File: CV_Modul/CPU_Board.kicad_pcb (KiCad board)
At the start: 4 copper layers, 65 x 100 mm, 123 parts, among them J101 Screw_Terminal_01x03, J102 Conn_02x01, J103 Conn_02x01, J104 Conn_01x08_Male, J105 Conn_02x09_Odd_Even, J106 Micro_SD_Card_Det, J107 Conn_01x06_Male, J108 Conn_02x01, J109 Conn_02x01, J110 Screw_Terminal_01x04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

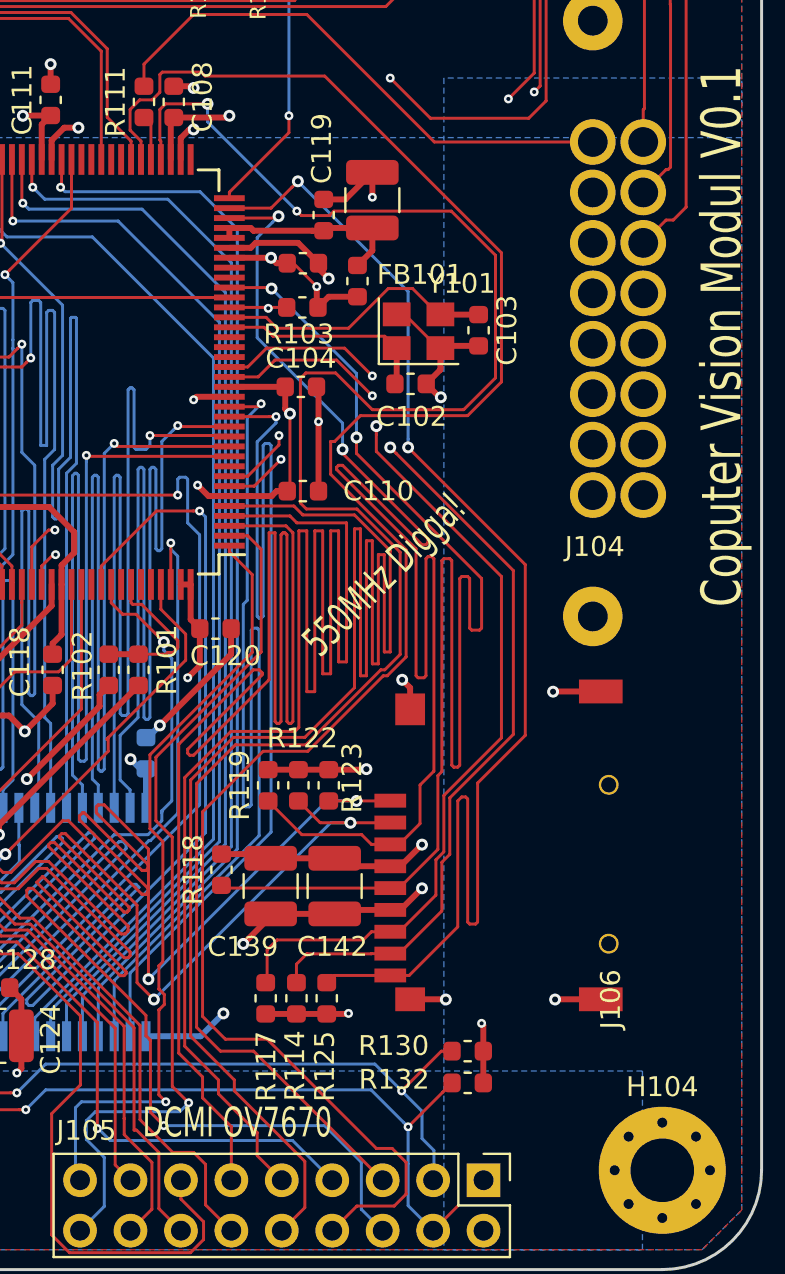
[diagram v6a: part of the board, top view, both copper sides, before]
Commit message: CV Modul Strong 1K Pulldown CAN Phy für Fast Mode. STEP Modelle hinzugefügt. Connector für Kamera etwas nach rechts verschoben
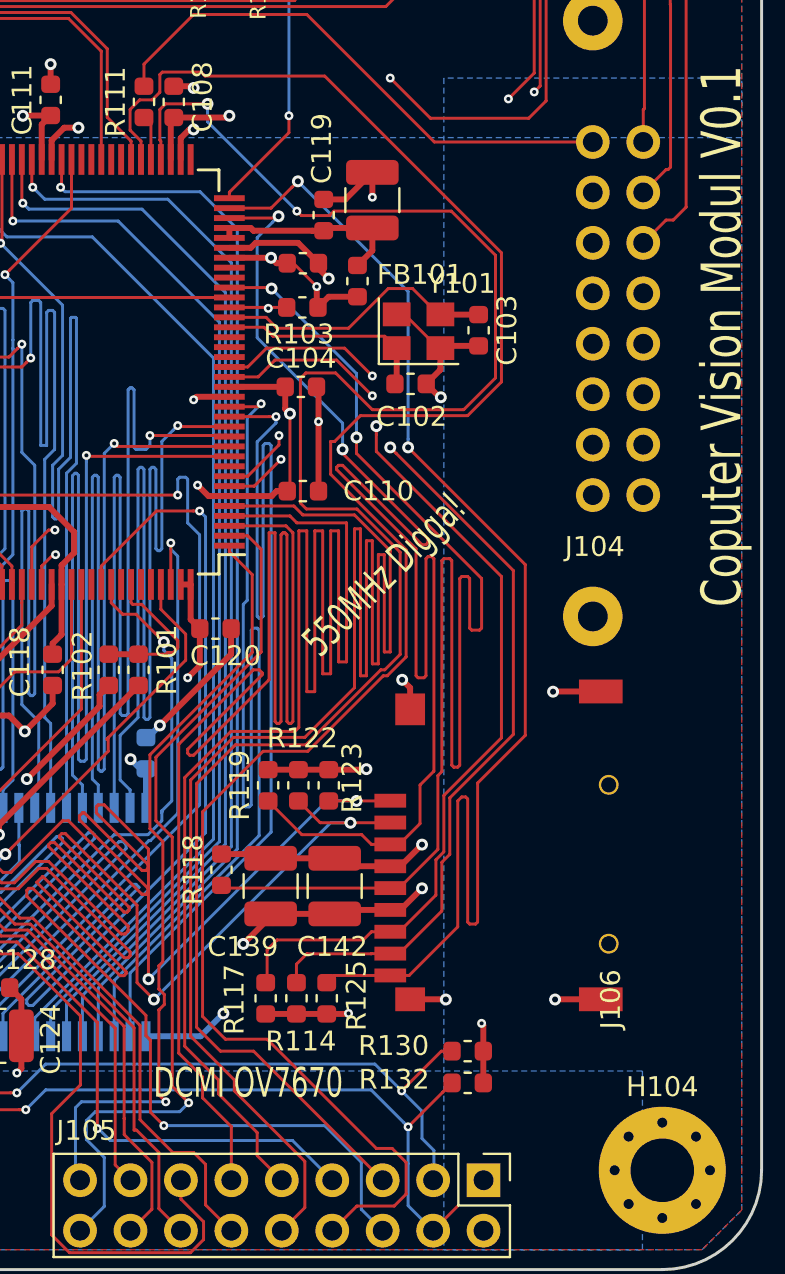
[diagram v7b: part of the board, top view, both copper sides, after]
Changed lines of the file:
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@@
     (add_net /NRST)
   )
+  (module ProjectFootprints:ST7789_Waveshare (layer F.Cu)
+    (at 126.5 111)
+    (fp_text reference J104 (at 0.1 2.6) (layer F.SilkS)
+      (effects (font (size 1 1) (thickness 0.15)))
+    )
+    (fp_text value Conn_01x08_Male (at -5 7.5) (layer F.Fab)
+      (effects (font (size 1 1) (thickness 0.15)))
+    )
+    (fp_line (start 2.5 -26.39) (end -55.5 -26.39) (layer Dwgs.User) (width 0.1))
+    (fp_line (start -55.5 -26.39) (end -55.5 8.61) (layer Dwgs.User) (width 0.1))
+    (fp_line (start -55.5 8.61) (end 2.5 8.61) (layer Dwgs.User) (width 0.1))
+    (fp_line (start 2.5 8.61) (end 2.5 -26.39) (layer Dwgs.User) (width 0.1))
+    (pad 16 thru_hole circle (at 2.54 0) (size 1.7 1.7) (drill 1) (layers *.Cu *.Mask))
+    (pad 15 thru_hole circle (at 2.54 -2.54) (size 1.7 1.7) (drill 1) (layers *.Cu *.Mask))
+    (pad 14 thru_hole circle (at 2.54 -5.08) (size 1.7 1.7) (drill 1) (layers *.Cu *.Mask))
+    (pad 13 thru_hole circle (at 2.54 -7.62) (size 1.7 1.7) (drill 1) (layers *.Cu *.Mask))
+    (pad 12 thru_hole circle (at 2.54 -10.16) (size 1.7 1.7) (drill 1) (layers *.Cu *.Mask))
+    (pad 11 thru_hole circle (at 2.54 -12.7) (size 1.7 1.7) (drill 1) (layers *.Cu *.Mask)
+      (net 58 /PA2))
+    (pad 10 thru_hole circle (at 2.54 -15.24) (size 1.7 1.7) (drill 1) (layers *.Cu *.Mask)
+      (net 106 /PC6))
+    (pad 9 thru_hole circle (at 2.54 -17.78) (size 1.7 1.7) (drill 1) (layers *.Cu *.Mask)
+      (net 9 /PC7))
+    (pad "" np_thru_hole circle (at -53 6.11) (size 3 3) (drill 1.5) (layers *.Cu *.Mask))
+    (pad "" np_thru_hole circle (at 0 6.11) (size 3 3) (drill 1.5) (layers *.Cu *.Mask))
+    (pad "" np_thru_hole circle (at -53 -23.89) (size 3 3) (drill 1.5) (layers *.Cu *.Mask))
+    (pad "" np_thru_hole circle (at 0 -23.89) (size 3 3) (drill 1.5) (layers *.Cu *.Mask))
+    (pad 8 thru_hole circle (at 0 -17.78) (size 1.7 1.7) (drill 1) (layers *.Cu *.Mask)
+      (net 26 /DISP_BL))
+    (pad 7 thru_hole circle (at 0 -15.24) (size 1.7 1.7) (drill 1) (layers *.Cu *.Mask)
+      (net 25 /DISP_RST))
+    (pad 6 thru_hole circle (at 0 -12.7) (size 1.7 1.7) (drill 1) (layers *.Cu *.Mask)
+      (net 24 /DISP_DC))
+    (pad 5 thru_hole circle (at 0 -10.16) (size 1.7 1.7) (drill 1) (layers *.Cu *.Mask)
+      (net 23 /DISP_CD))
+    (pad 4 thru_hole circle (at 0 -7.62) (size 1.7 1.7) (drill 1) (layers *.Cu *.Mask)
+      (net 22 /DISP_CLK))
+    (pad 3 thru_hole circle (at 0 -5.08) (size 1.7 1.7) (drill 1) (layers *.Cu *.Mask)
+      (net 21 /DISP_DIN))
+    (pad 2 thru_hole circle (at 0 -2.54) (size 1.7 1.7) (drill 1) (layers *.Cu *.Mask)
+      (net 1 GND))
+    (pad 1 thru_hole circle (at 0 0) (size 1.7 1.7) (drill 1) (layers *.Cu *.Mask)
+      (net 5 +3V3))
+  )
   (module Connector_PinHeader_2.54mm:PinHeader_2x09_P2.54mm_Vertical (layer F.Cu)
     (at 121 145.5 270)
@@
     (pad 18 thru_hole oval (at 2.54 20.32 270) (size 1.7 1.7) (drill 1) (layers *.Cu *.Mask)
       (net 41 /CAM_RESET))
-    (model ${KISYS3DMOD}/Connector_PinHeader_2.54mm.3dshapes/PinHeader_2x09_P2.54mm_Vertical.wrl
+    (model "${KIPRJMOD}/KiCAD_Library/STEP/18-Pin Shrouded Header (IDC) Straight.stp"
       (at (xyz 0 0 0))
       (scale (xyz 1 1 1))
-      (rotate (xyz 0 0 0))
+      (rotate (xyz 0 0 -90))
     )
   )
@@
     (fp_line (start 0 0) (end 1 0) (layer Dwgs.User) (width 0.12))
   )
-  (module ProjectFootprints:ST7789_Waveshare (layer F.Cu)
-    (at 126.5 111)
-    (fp_text reference J104 (at 0.1 2.6) (layer F.SilkS)
-      (effects (font (size 1 1) (thickness 0.15)))
-    )
-    (fp_text value Conn_01x08_Male (at -5 7.5) (layer F.Fab)
-      (effects (font (size 1 1) (thickness 0.15)))
-    )
-    (fp_line (start 2.5 -26.39) (end -55.5 -26.39) (layer Dwgs.User) (width 0.1))
-    (fp_line (start -55.5 -26.39) (end -55.5 8.61) (layer Dwgs.User) (width 0.1))
-    (fp_line (start -55.5 8.61) (end 2.5 8.61) (layer Dwgs.User) (width 0.1))
-    (fp_line (start 2.5 8.61) (end 2.5 -26.39) (layer Dwgs.User) (width 0.1))
-    (pad 16 thru_hole circle (at 2.54 0) (size 2.3 2.3) (drill 1.5) (layers *.Cu *.Mask))
-    (pad 15 thru_hole circle (at 2.54 -2.54) (size 2.3 2.3) (drill 1.5) (layers *.Cu *.Mask))
-    (pad 14 thru_hole circle (at 2.54 -5.08) (size 2.3 2.3) (drill 1.5) (layers *.Cu *.Mask))
-    (pad 13 thru_hole circle (at 2.54 -7.62) (size 2.3 2.3) (drill 1.5) (layers *.Cu *.Mask))
-    (pad 12 thru_hole circle (at 2.54 -10.16) (size 2.3 2.3) (drill 1.5) (layers *.Cu *.Mask))
-    (pad 11 thru_hole circle (at 2.54 -12.7) (size 2.3 2.3) (drill 1.5) (layers *.Cu *.Mask)
-      (net 58 /PA2))
-    (pad 10 thru_hole circle (at 2.54 -15.24) (size 2.3 2.3) (drill 1.5) (layers *.Cu *.Mask)
-      (net 106 /PC6))
-    (pad 9 thru_hole circle (at 2.54 -17.78) (size 2.3 2.3) (drill 1.5) (layers *.Cu *.Mask)
-      (net 9 /PC7))
-    (pad "" np_thru_hole circle (at -53 6.11) (size 3 3) (drill 1.5) (layers *.Cu *.Mask))
-    (pad "" np_thru_hole circle (at 0 6.11) (size 3 3) (drill 1.5) (layers *.Cu *.Mask))
-    (pad "" np_thru_hole circle (at -53 -23.89) (size 3 3) (drill 1.5) (layers *.Cu *.Mask))
-    (pad "" np_thru_hole circle (at 0 -23.89) (size 3 3) (drill 1.5) (layers *.Cu *.Mask))
-    (pad 8 thru_hole circle (at 0 -17.78) (size 2.3 2.3) (drill 1.5) (layers *.Cu *.Mask)
-      (net 26 /DISP_BL))
-    (pad 7 thru_hole circle (at 0 -15.24) (size 2.3 2.3) (drill 1.5) (layers *.Cu *.Mask)
-      (net 25 /DISP_RST))
-    (pad 6 thru_hole circle (at 0 -12.7) (size 2.3 2.3) (drill 1.5) (layers *.Cu *.Mask)
-      (net 24 /DISP_DC))
-    (pad 5 thru_hole circle (at 0 -10.16) (size 2.3 2.3) (drill 1.5) (layers *.Cu *.Mask)
-      (net 23 /DISP_CD))
-    (pad 4 thru_hole circle (at 0 -7.62) (size 2.3 2.3) (drill 1.5) (layers *.Cu *.Mask)
-      (net 22 /DISP_CLK))
-    (pad 3 thru_hole circle (at 0 -5.08) (size 2.3 2.3) (drill 1.5) (layers *.Cu *.Mask)
-      (net 21 /DISP_DIN))
-    (pad 2 thru_hole circle (at 0 -2.54) (size 2.3 2.3) (drill 1.5) (layers *.Cu *.Mask)
-      (net 1 GND))
-    (pad 1 thru_hole circle (at 0 0) (size 2.3 2.3) (drill 1.5) (layers *.Cu *.Mask)
-      (net 5 +3V3))
-  )
   (module ProjectFootprints:L_CommonModeChoke_Coilcraft_1812CAN (layer F.Cu)
     (at 105.6 66.2)
@@
     (pad 3 thru_hole circle (at 10 0 180) (size 2.1 2.1) (drill 1.1) (layers *.Cu *.Mask)
       (net 1 GND))
-    (model ${KISYS3DMOD}/TerminalBlock_RND.3dshapes/TerminalBlock_RND_205-00046_1x03_P5.00mm_Horizontal.wrl
-      (at (xyz 0 0 0))
+    (model ${KIPRJMOD}/KiCAD_Library/STEP/DG306-5.0-03P-12-00AH.STEP
+      (offset (xyz 12.5 -4.5 0))
       (scale (xyz 1 1 1))
-      (rotate (xyz 0 0 0))
+      (rotate (xyz -90 0 180))
     )
   )
@@
     (pad 4 thru_hole circle (at 15 0) (size 2.1 2.1) (drill 1.1) (layers *.Cu *.Mask)
       (net 109 /CAN_L))
-    (model ${KISYS3DMOD}/TerminalBlock_RND.3dshapes/TerminalBlock_RND_205-00047_1x04_P5.00mm_Horizontal.wrl
-      (at (xyz 0 0 0))
+    (model ${KIPRJMOD}/KiCAD_Library/STEP/DG306-5.0-04P-12-00AH.STEP
+      (offset (xyz 17.5 -4.5 0))
       (scale (xyz 1 1 1))
-      (rotate (xyz 0 0 0))
+      (rotate (xyz -90 0 180))
     )
   )
@@
     (tags resistor)
     (attr smd)
-    (fp_text reference R125 (at -3.425 -0.1 90) (layer F.SilkS)
+    (fp_text reference R125 (at 0.139133 1.497635 90) (layer F.SilkS)
       (effects (font (size 1 1) (thickness 0.15)))
     )
@@
     (tags resistor)
     (attr smd)
-    (fp_text reference R114 (at 3.4 0.075 270) (layer F.SilkS)
+    (fp_text reference R114 (at 2.160867 -0.222635) (layer F.SilkS)
       (effects (font (size 1 1) (thickness 0.15)))
     )
@@
     (tags resistor)
     (attr smd)
-    (fp_text reference R117 (at 3.425 -0.025 270) (layer F.SilkS)
+    (fp_text reference R117 (at 0.060867 1.577365 270) (layer F.SilkS)
       (effects (font (size 1 1) (thickness 0.15)))
     )
@@
     (effects (font (size 1.5 1.5) (thickness 0.15)))
   )
-  (gr_text "DCMI OV7670" (at 108.6 142.6) (layer F.SilkS)
+  (gr_text "DCMI OV7670" (at 109.15 140.6) (layer F.SilkS)
     (effects (font (size 1.5 1) (thickness 0.15)))
   )

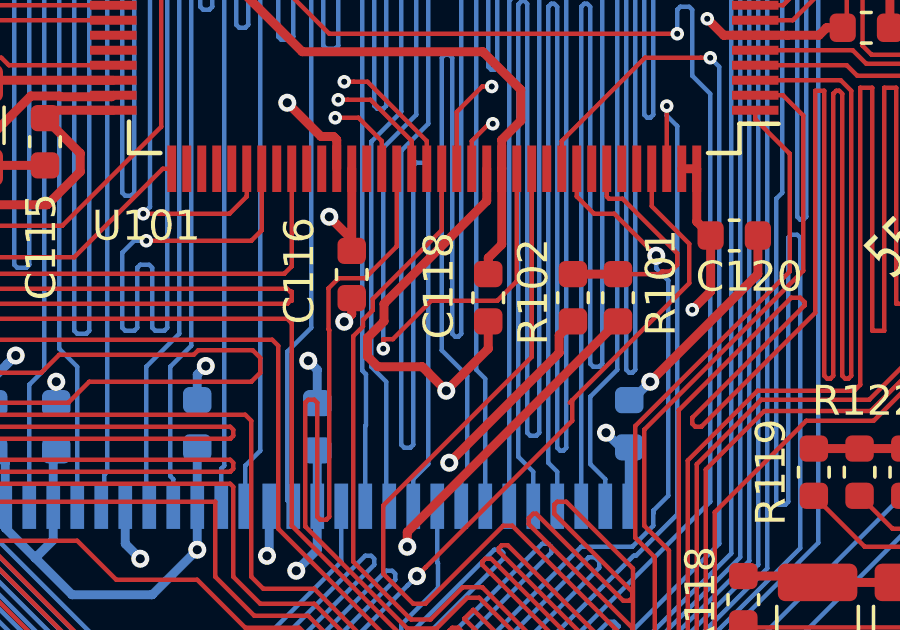
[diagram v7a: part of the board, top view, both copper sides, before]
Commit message: ESD Protection für Feeder Modul USB hinzugefügt, Status LED für Controller Modul hinzugefügt
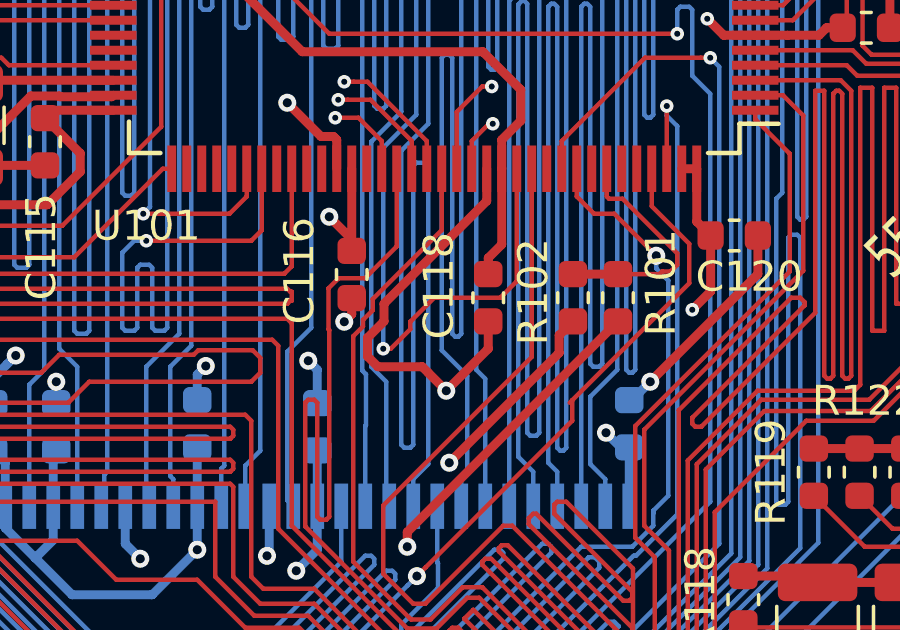
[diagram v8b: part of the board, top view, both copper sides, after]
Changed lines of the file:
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@@
     (thickness 1.6)
     (drawings 28)
-    (tracks 2272)
+    (tracks 2273)
     (zones 0)
     (modules 123)
@@
   (segment (start 88.6 101.4) (end 88.6 120.8) (width 0.15) (layer B.Cu) (net 96) (status 40000))
   (segment (start 88.9 101.3) (end 88.7 101.3) (width 0.15) (layer B.Cu) (net 96) (status 40000))
-  (via (at 95.8 121.5) (size 0.45) (drill 0.2) (layers F.Cu B.Cu) (net 97) (status 40000))
+  (via (at 95.8 121.5) (size 0.45) (drill 0.2) (layers F.Cu B.Cu) (net 97))
   (segment (start 95.8 114.8) (end 95.8 121.5) (width 0.15) (layer B.Cu) (net 97) (status 40000))
   (segment (start 96.9 113.7) (end 95.8 114.8) (width 0.15) (layer B.Cu) (net 97) (status 40000))
@@
   (segment (start 96.4 113.6) (end 96.4 101.7) (width 0.15) (layer B.Cu) (net 97) (status 40000))
   (segment (start 96.5 101.6) (end 96.8 101.6) (width 0.15) (layer B.Cu) (net 97) (status 40000))
-  (segment (start 95.8 121.181802) (end 95.8 121.5) (width 0.15) (layer F.Cu) (net 97) (status 40000))
-  (segment (start 96.118198 121.181802) (end 95.8 121.181802) (width 0.15) (layer F.Cu) (net 97) (status 40000))
-  (segment (start 97.4 119.9) (end 96.118198 121.181802) (width 0.15) (layer F.Cu) (net 97) (status 40000))
-  (segment (start 100.25 115.5) (end 100.25 119.25) (width 0.15) (layer F.Cu) (net 97) (status 40000))
-  (segment (start 99.6 119.9) (end 97.4 119.9) (width 0.15) (layer F.Cu) (net 97) (status 40000))
-  (segment (start 100.25 119.25) (end 99.6 119.9) (width 0.15) (layer F.Cu) (net 97) (status 40000))
+  (segment (start 96.05 121.5) (end 95.8 121.5) (width 0.15) (layer F.Cu) (net 97))
+  (segment (start 100.25 119.25) (end 99.7 119.8) (width 0.15) (layer F.Cu) (net 97))
+  (segment (start 100.25 115.5) (end 100.25 119.25) (width 0.15) (layer F.Cu) (net 97))
+  (segment (start 99.7 119.8) (end 97.5 119.8) (width 0.15) (layer F.Cu) (net 97))
+  (segment (start 97.5 119.8) (end 96.7 120.6) (width 0.15) (layer F.Cu) (net 97))
+  (segment (start 96.7 120.6) (end 96.7 120.85) (width 0.15) (layer F.Cu) (net 97))
+  (segment (start 96.7 120.85) (end 96.05 121.5) (width 0.15) (layer F.Cu) (net 97))
   (via (at 106.7 111.799996) (size 0.45) (drill 0.2) (layers F.Cu B.Cu) (net 98) (status 40000))
   (segment (start 101.75 115.5) (end 101.75 114.575) (width 0.15) (layer F.Cu) (net 98) (status 40000))
